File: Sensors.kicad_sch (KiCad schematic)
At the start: 20 parts, among them IC2 MAX-M10S-00B, IC3 ADXL375BCCZ-RL, IC4 ASM330LHHTR, J7 Conn_Coaxial, U4 LPS22HH, U5 LSM303C

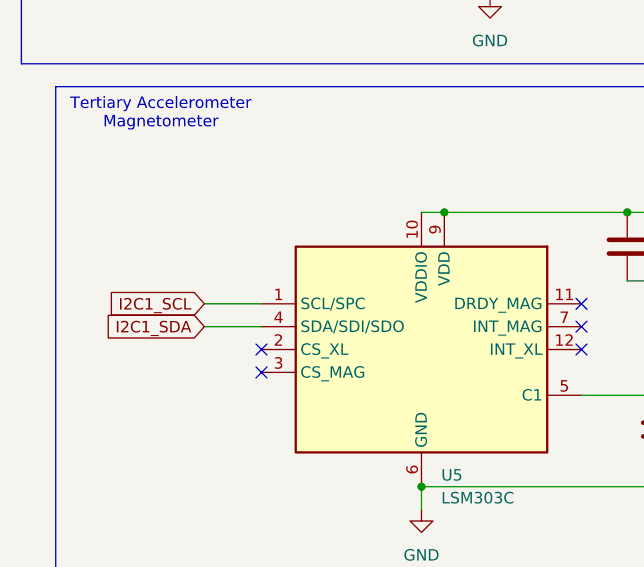
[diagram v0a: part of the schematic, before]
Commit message: Fixed major sensor connection error, ADXL still requires investigation
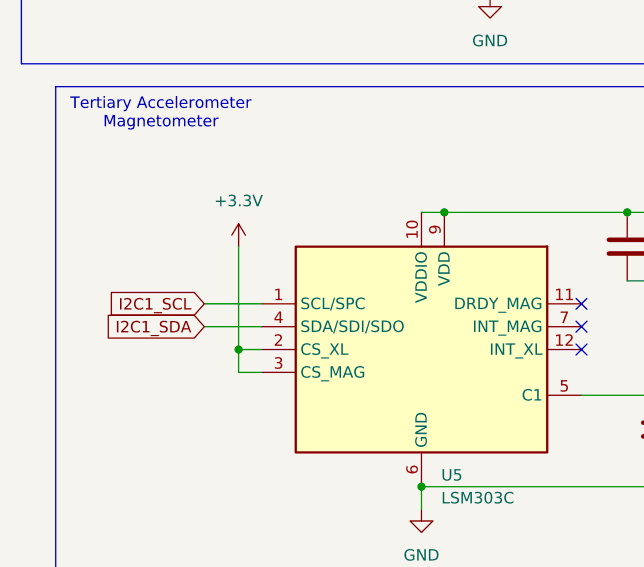
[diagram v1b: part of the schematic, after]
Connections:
- net +3.3V: now also U5.2 (CS_XL), U5.3 (CS_MAG)
- no-connect marks 20 -> 18
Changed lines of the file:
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@@
 	)
 	(junction
+		(at 38.1 168.91)
+		(diameter 0)
+		(color 0 0 0 0)
+	)
+	(junction
 		(at 60.96 153.67)
 		(diameter 0)
@@
 	)
 	(no_connect
-		(at 40.64 168.91)
-	)
-	(no_connect
 		(at 247.65 127)
 	)
 	(no_connect
-		(at 40.64 171.45)
-	)
-	(no_connect
 		(at 91.44 113.03)
 	)
@@
 	(wire
 		(pts
+			(xy 38.1 168.91) (xy 40.64 168.91)
+		)
+		(stroke
+			(width 0)
+			(type default)
+		)
+	)
+	(wire
+		(pts
 			(xy 68.58 128.27) (xy 68.58 127)
 		)
@@
 	(wire
 		(pts
+			(xy 38.1 171.45) (xy 38.1 168.91)
+		)
+		(stroke
+			(width 0)
+			(type default)
+		)
+	)
+	(wire
+		(pts
 			(xy 200.66 132.08) (xy 204.47 132.08)
 		)
@@
 	(wire
 		(pts
+			(xy 38.1 168.91) (xy 38.1 157.48)
+		)
+		(stroke
+			(width 0)
+			(type default)
+		)
+	)
+	(wire
+		(pts
 			(xy 115.57 101.6) (xy 115.57 104.14)
 		)
@@
 	(wire
 		(pts
+			(xy 40.64 171.45) (xy 38.1 171.45)
+		)
+		(stroke
+			(width 0)
+			(type default)
+		)
+	)
+	(wire
+		(pts
 			(xy 144.78 58.42) (xy 157.48 58.42)
 		)
@@
 					(unit 1)
 				)
+			)
+		)
+	)
+	(symbol
+		(lib_id "power:+3.3V")
+		(at 38.1 157.48 0)
+		(unit 1)
+		(exclude_from_sim no)
+		(in_bom yes)
+		(on_board yes)
+		(dnp no)
+		(fields_autoplaced yes)
+		(property "Reference" "#PWR074"
+			(at 38.1 161.29 0)
+			(effects
+				(font
+					(size 1.27 1.27)
+				)
+				(hide yes)
+			)
+		)
+		(property "Value" "+3.3V"
+			(at 38.1 152.4 0)
+			(effects
+				(font
+					(size 1.27 1.27)
+				)
+			)
+		)
+		(property "Footprint" ""
+			(at 38.1 157.48 0)
+			(effects
+				(font
+					(size 1.27 1.27)
+				)
+				(hide yes)
+			)
+		)
+		(property "Datasheet" ""
+			(at 38.1 157.48 0)
+			(effects
+				(font
+					(size 1.27 1.27)
+				)
+				(hide yes)
+			)
+		)
+		(property "Description" "Power symbol creates a global label with name \"+3.3V\""
+			(at 38.1 157.48 0)
+			(effects
+				(font
+					(size 1.27 1.27)
+				)
+				(hide yes)
+			)
+		)
+		(pin "1"
+		)
+		(instances
+			(project "Vanguard"
+				(path "/3eaebd91-5a76-469f-9e30-3d62ffb5c6ad/3fe83357-6c53-4f1f-b41b-54e8ba2f9ff3"
+					(reference "#PWR074")
+					(unit 1)
+				)
